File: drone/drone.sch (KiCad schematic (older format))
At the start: 1 part

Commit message: Schematic
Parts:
- added X?: CRYSTAL, symbol CRYSTAL
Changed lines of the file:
@@
 LIBS:contrib
 LIBS:valves
+LIBS:drone-cache
 EELAYER 24 0
 EELAYER END
@@
 Wire Wire Line
 	3725 4850 3725 4800
+$Comp
+L CRYSTAL X?
+U 1 1 556BC952
+P 2000 3475
+F 0 "X?" H 2000 3625 60  0000 C CNN
+F 1 "CRYSTAL" H 2000 3325 60  0000 C CNN
+F 2 "" H 2000 3475 60  0000 C CNN
+F 3 "" H 2000 3475 60  0000 C CNN
+	1    2000 3475
+	0    -1   -1   0
+$EndComp
 $EndSCHEMATC

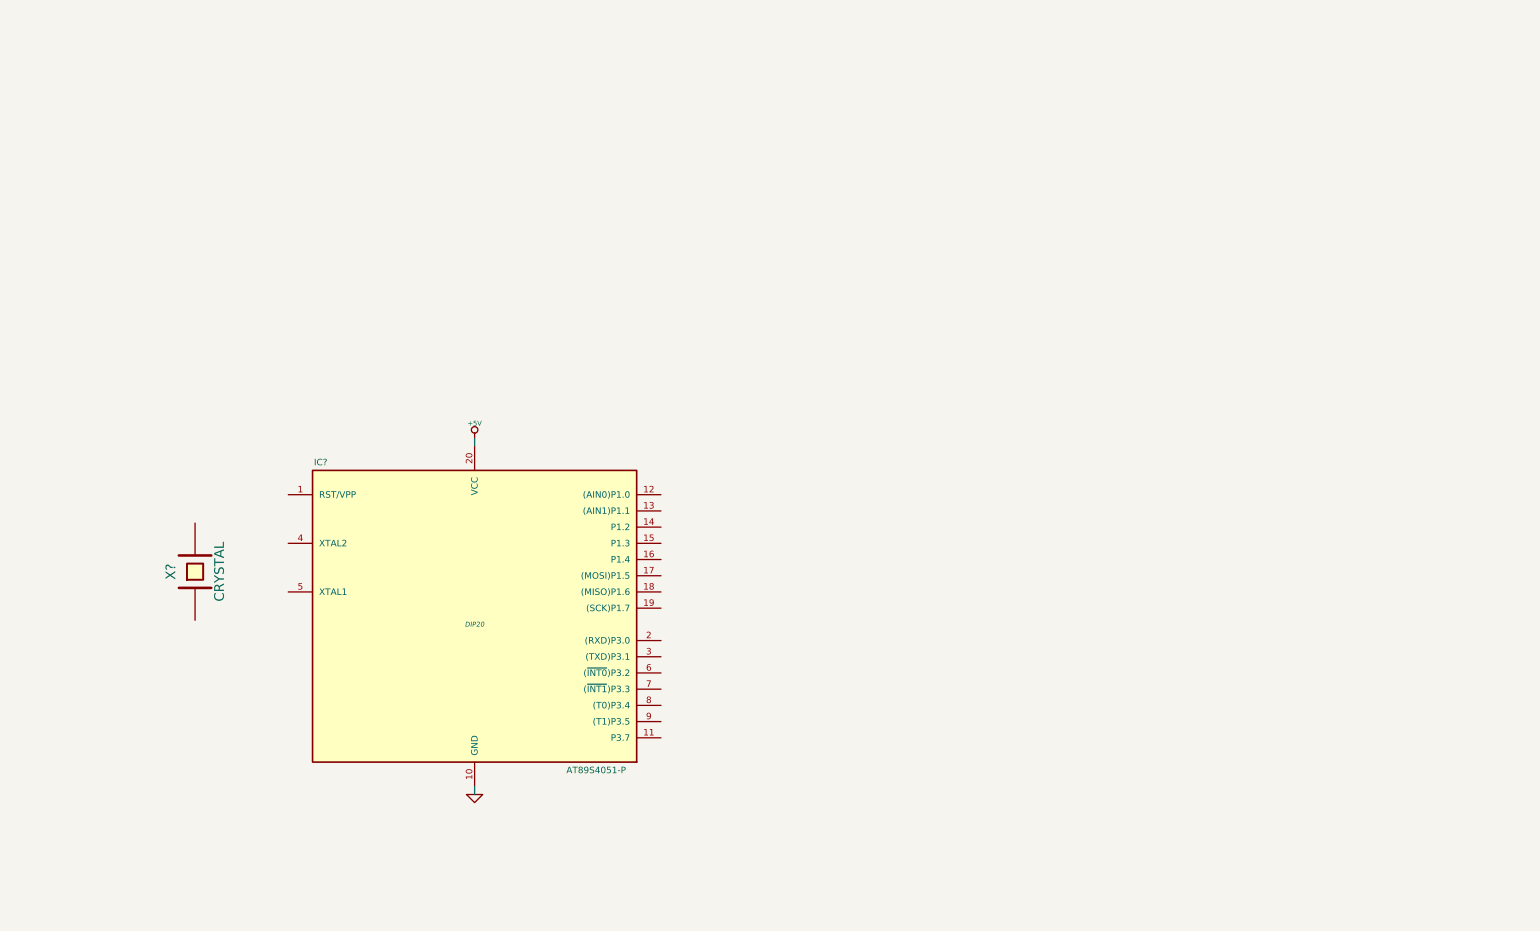
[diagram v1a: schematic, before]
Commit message: Worked on the drone
* Added the assembly files
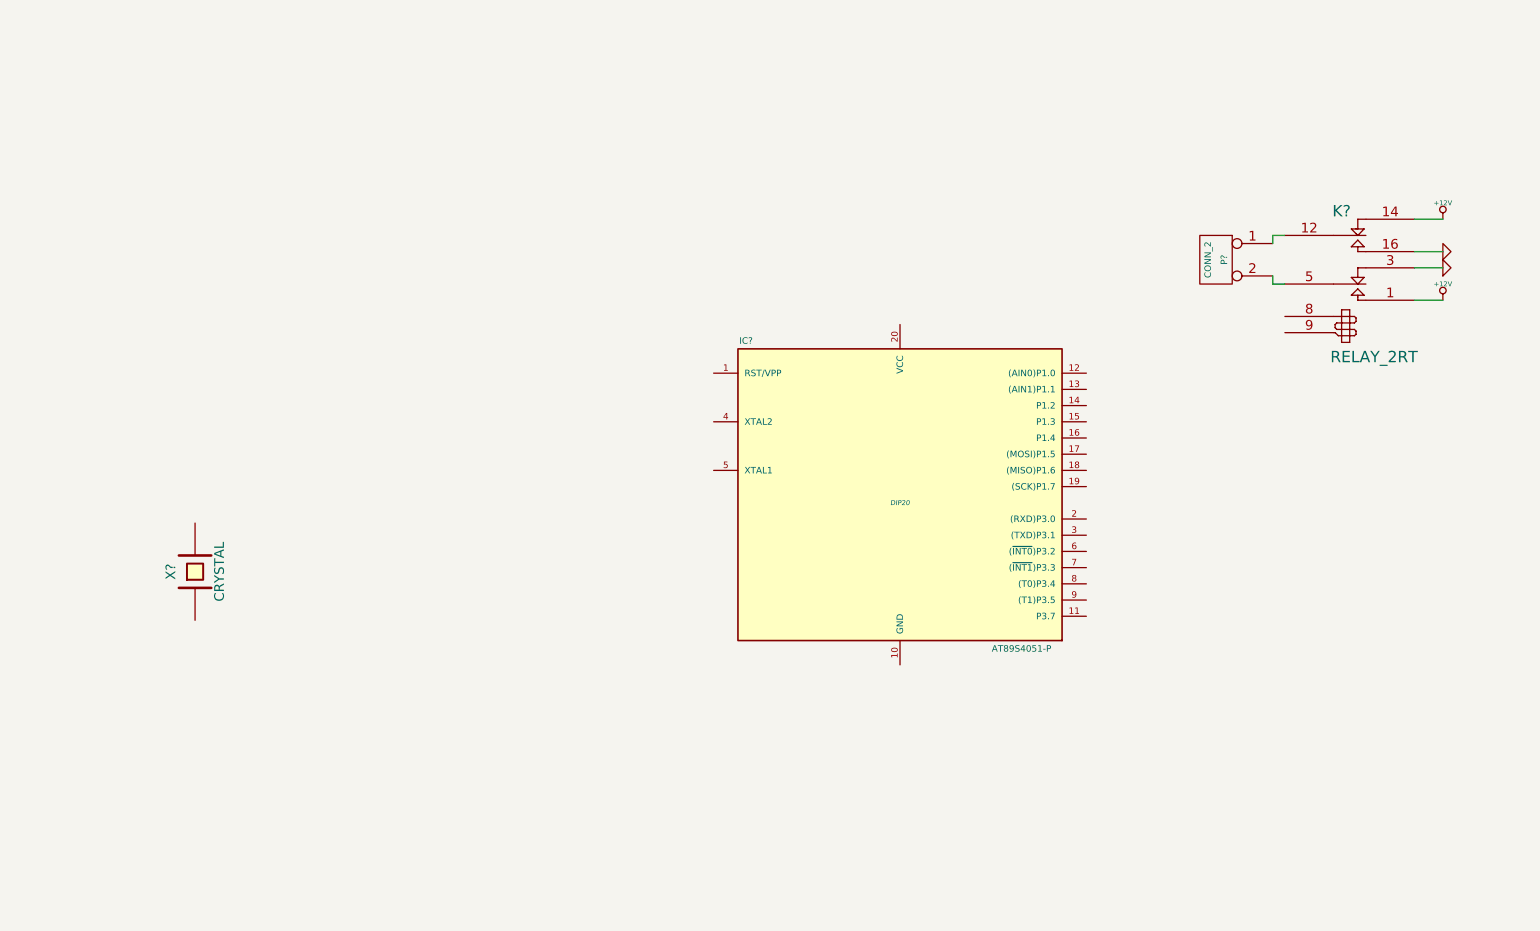
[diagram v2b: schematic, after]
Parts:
- removed IC?: AT89S4051-P, DIP20, symbol AT89S4051-P
- added IC?: AT89S4051-P, DIP20, symbol AT89S4051-P
- added K?: RELAY_2RT, symbol RELAY_2RT
- added P?: CONN_2, symbol CONN_2
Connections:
- net GND: now also K?.16 (T2), K?.3 (R1)
- new net: K?.12 (C2), P?.1 (P1)
- new net: K?.5 (C1), P?.2 (PM)
- new net +12V: K?.1 (T1), K?.14 (R2)
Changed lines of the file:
@@
 $EndDescr
-$Comp
-L AT89S4051-P IC?
-U 1 1 556BB736
-P 3725 3800
-F 0 "IC?" H 2775 4800 40  0000 C CNN
-F 1 "AT89S4051-P" H 4475 2900 40  0000 C CNN
-F 2 "DIP20" H 3725 3800 30  0000 C CIN
-F 3 "" H 3725 3800 60  0000 C CNN
-	1    3725 3800
-	1    0    0    -1
-$EndComp
-$Comp
-L +5V #PWR?
-U 1 1 556BB808
-P 3725 2650
-F 0 "#PWR?" H 3725 2740 20  0001 C CNN
-F 1 "+5V" H 3725 2740 30  0000 C CNN
-F 2 "" H 3725 2650 60  0000 C CNN
-F 3 "" H 3725 2650 60  0000 C CNN
-	1    3725 2650
-	1    0    0    -1
-$EndComp
-Wire Wire Line
-	3725 2700 3725 2650
-$Comp
-L GND #PWR?
-U 1 1 556BB82E
-P 3725 4850
-F 0 "#PWR?" H 3725 4850 30  0001 C CNN
-F 1 "GND" H 3725 4780 30  0001 C CNN
-F 2 "" H 3725 4850 60  0000 C CNN
-F 3 "" H 3725 4850 60  0000 C CNN
-	1    3725 4850
-	1    0    0    -1
-$EndComp
-Wire Wire Line
-	3725 4850 3725 4800
 $Comp
 L CRYSTAL X?
@@
 	0    -1   -1   0
 $EndComp
+$Comp
+L AT89S4051-P IC?
+U 1 1 556CD57A
+P 6350 3050
+F 0 "IC?" H 5400 4050 40  0000 C CNN
+F 1 "AT89S4051-P" H 7100 2150 40  0000 C CNN
+F 2 "DIP20" H 6350 3050 30  0000 C CIN
+F 3 "" H 6350 3050 60  0000 C CNN
+	1    6350 3050
+	1    0    0    -1
+$EndComp
+$Comp
+L RELAY_2RT K?
+U 1 1 556CD7C9
+P 9125 1650
+F 0 "K?" H 9075 2050 70  0000 C CNN
+F 1 "RELAY_2RT" H 9275 1150 70  0000 C CNN
+F 2 "" H 9125 1650 60  0000 C CNN
+F 3 "" H 9125 1650 60  0000 C CNN
+	1    9125 1650
+	1    0    0    -1
+$EndComp
+$Comp
+L CONN_2 P?
+U 1 1 556CD7F2
+P 8300 1550
+F 0 "P?" V 8250 1550 40  0000 C CNN
+F 1 "CONN_2" V 8350 1550 40  0000 C CNN
+F 2 "" H 8300 1550 60  0000 C CNN
+F 3 "" H 8300 1550 60  0000 C CNN
+	1    8300 1550
+	-1   0    0    -1
+$EndComp
+$Comp
+L +12V #PWR?
+U 1 1 556CD84C
+P 9700 1300
+F 0 "#PWR?" H 9700 1250 20  0001 C CNN
+F 1 "+12V" H 9700 1400 30  0000 C CNN
+F 2 "" H 9700 1300 60  0000 C CNN
+F 3 "" H 9700 1300 60  0000 C CNN
+	1    9700 1300
+	1    0    0    -1
+$EndComp
+$Comp
+L +12V #PWR?
+U 1 1 556CD860
+P 9700 1800
+F 0 "#PWR?" H 9700 1750 20  0001 C CNN
+F 1 "+12V" H 9700 1900 30  0000 C CNN
+F 2 "" H 9700 1800 60  0000 C CNN
+F 3 "" H 9700 1800 60  0000 C CNN
+	1    9700 1800
+	1    0    0    -1
+$EndComp
+Wire Wire Line
+	9525 1800 9700 1800
+Wire Wire Line
+	9525 1300 9700 1300
+$Comp
+L GND #PWR?
+U 1 1 556CD879
+P 9700 1500
+F 0 "#PWR?" H 9700 1500 30  0001 C CNN
+F 1 "GND" H 9700 1430 30  0001 C CNN
+F 2 "" H 9700 1500 60  0000 C CNN
+F 3 "" H 9700 1500 60  0000 C CNN
+	1    9700 1500
+	0    -1   -1   0
+$EndComp
+$Comp
+L GND #PWR?
+U 1 1 556CD88D
+P 9700 1600
+F 0 "#PWR?" H 9700 1600 30  0001 C CNN
+F 1 "GND" H 9700 1530 30  0001 C CNN
+F 2 "" H 9700 1600 60  0000 C CNN
+F 3 "" H 9700 1600 60  0000 C CNN
+	1    9700 1600
+	0    -1   -1   0
+$EndComp
+Wire Wire Line
+	9525 1600 9700 1600
+Wire Wire Line
+	9700 1500 9525 1500
+Wire Wire Line
+	8650 1450 8650 1400
+Wire Wire Line
+	8650 1400 8725 1400
+Wire Wire Line
+	8650 1650 8650 1700
+Wire Wire Line
+	8650 1700 8725 1700
 $EndSCHEMATC

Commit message: Worked on the drone schematic
* Wrote some code
    * Setup interupts for the controller
    * Wrote basic framework of code
* Worked on the schematic
    * Placed parts
    * Made notes
    * Figured out where some things go
    * Blah Blah
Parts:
- added C? (x2): 5pF, symbol C
- added Q1: NPN, symbol NPN
- added R1: R, symbol R
- added SW?: SW_PUSH_SMALL, symbol SW_PUSH_SMALL
- gave numbers to parts that had none: 4
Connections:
- net GND: now also IC1.10 (GND), K1.9, C?.1, C?.1
- net at X1.1: now also IC1.5 (XTAL1), C?.2
- net at X1.2: now also IC1.4 (XTAL2), C?.2
- net at IC1.1 (RST/VPP): now also SW?.2
- net MainMotorRev: now reaches IC1.11 (P3.7)
- net at K1.8: now also Q1.1 (E)
- new net: Q1.2 (B), R1.1
- new net +5V: Q1.3 (C), SW?.1
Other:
- note added: "Primary Drive Motor\nConnects Here\n"
- moved on the sheet: IC1, K1, P1, X1

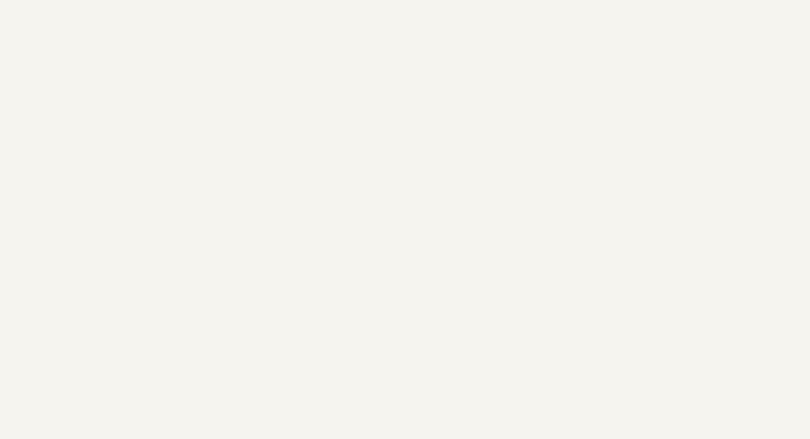
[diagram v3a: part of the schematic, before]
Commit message: Worked on the project some more
* Added L293NE to schematic lib
* Drew some more of the schematic
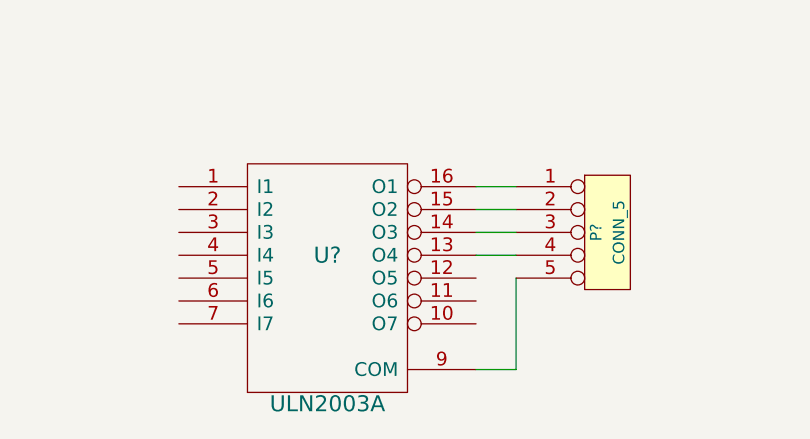
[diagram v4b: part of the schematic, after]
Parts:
- added P?: CONN_5, symbol CONN_5
- added U?: ULN2003A, symbol ULN2003A
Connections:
- net GND: now also U?.8 (GND)
- new net: P?.4, U?.13 (O4)
- new net: P?.3, U?.14 (O3)
- new net: P?.2, U?.15 (O2)
- new net: P?.1, U?.16 (O1)
- new net: P?.5, U?.9 (COM)
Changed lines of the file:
@@
 	1    0    0    -1
 $EndComp
+$Comp
+L ULN2003A U?
+U 1 1 556D0DB4
+P 5500 4625
+F 0 "U?" H 5500 4725 70  0000 C CNN
+F 1 "ULN2003A" H 5500 4075 70  0000 C CNN
+F 2 "" H 5500 4625 60  0000 C CNN
+F 3 "" H 5500 4625 60  0000 C CNN
+	1    5500 4625
+	1    0    0    -1
+$EndComp
+$Comp
+L CONN_5 P?
+U 1 1 556D0FC3
+P 6725 4425
+F 0 "P?" V 6675 4425 50  0000 C CNN
+F 1 "CONN_5" V 6775 4425 50  0000 C CNN
+F 2 "" H 6725 4425 60  0000 C CNN
+F 3 "" H 6725 4425 60  0000 C CNN
+	1    6725 4425
+	1    0    0    -1
+$EndComp
+Wire Wire Line
+	6325 4625 6325 5025
+Wire Wire Line
+	6325 5025 6150 5025
+Wire Wire Line
+	6150 4225 6325 4225
+Wire Wire Line
+	6325 4325 6150 4325
+Wire Wire Line
+	6150 4425 6325 4425
+Wire Wire Line
+	6150 4525 6325 4525
 $EndSCHEMATC

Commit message: Worked on the mower drone
* Drew more of the schematic
* Worked on the assmebly program
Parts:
- removed P?: CONN_5, symbol CONN_5
- removed U?: ULN2003A, symbol ULN2003A
- added K?: RELAY_2RT, symbol RELAY_2RT
- added P?: CONN_2, symbol CONN_2
- added P?: CONN_3X2, symbol CONN_3X2
- added Q?: NPN, symbol NPN
- added R?: 3k3, symbol R
- added SW? (x2): SW_PUSH, symbol SW_PUSH
- R?: renamed from R1; value R -> 3k3
- renumbered IC1 to IC?, K1 to K?, P1 to P?, Q1 to Q?, X1 to X?
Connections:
- net MainMotorRev is gone; now on net MotorRight: IC?.11 (P3.7)
- net +12V: now also K?.1 (T1), K?.14 (R2)
- net +5V: now also IC?.20 (VCC), P?.2, Q?.3 (C), SW?.2, SW?.2
- net GND: now also K?.16 (T2), K?.3 (R1), K?.9, P?.6
- net Reset: now reaches IC?.1 (RST/VPP), SW?.2
- net Reset: now also P?.5
- net at IC?.17 ((MOSI)P1.5): now also P?.4
- net at IC?.18 ((MISO)P1.6): now also P?.1
- net at IC?.19 ((SCK)P1.7): now also P?.3
- net Int0: now reaches IC?.6 ((~INT0~)P3.2)
- net Int0: now also SW?.1, SW?.1
- net MotorLeft: now reaches IC?.9 ((T1)P3.5)
- net MotorLeft: now also R?.2
- net MotorRight: now reaches R?.2
- new net: K?.12 (C2), P?.1 (P1)
- new net: K?.5 (C1), P?.2 (PM)
- new net: K?.8, Q?.1 (E)
- new net: Q?.2 (B), R?.1
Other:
- note added: "Bumper Switches"
- note added: "Left Drive Motor"
- note added: "Programming\nInterface"
- note added: "Reset Button"
- note added: "Right Drive Motor"
- note removed: "Primary Drive Motor\nConnects Here\n"
